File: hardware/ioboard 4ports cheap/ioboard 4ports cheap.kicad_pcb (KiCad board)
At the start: 2 copper layers, 106 x 60 mm, 38 parts, among them J1 Conn_02x06_Odd_Even, J2 Conn_01x03, J3 XLR3, J4 Conn_01x03, J5 XLR3, J6 Conn_01x03, J7 XLR3, J8 Conn_01x03, J9 XLR3, U1 M24C02-WMN, U2 SP3485EN, U3 SP3485EN, U4 SP3485EN, U5 SP3485EN

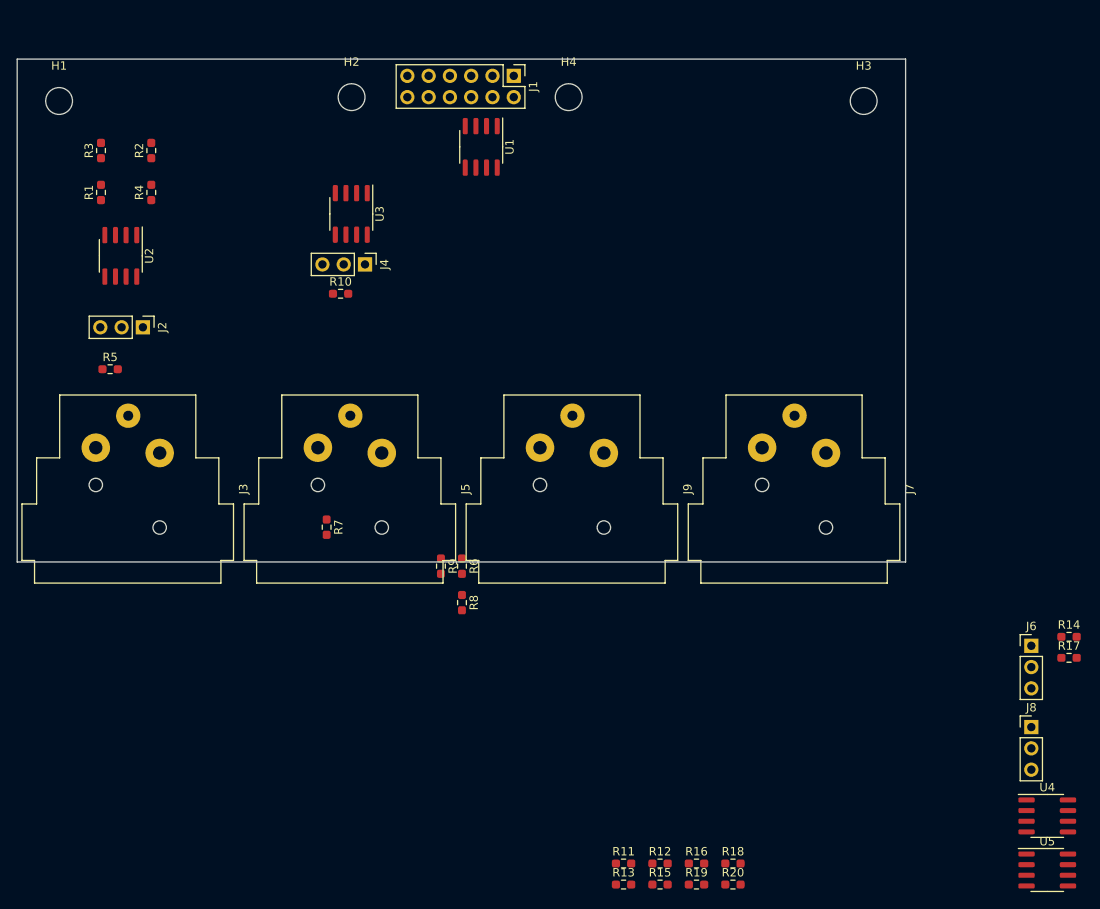
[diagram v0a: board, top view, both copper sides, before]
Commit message: Re-work ioboard 4ports cheap. Should be production-ready
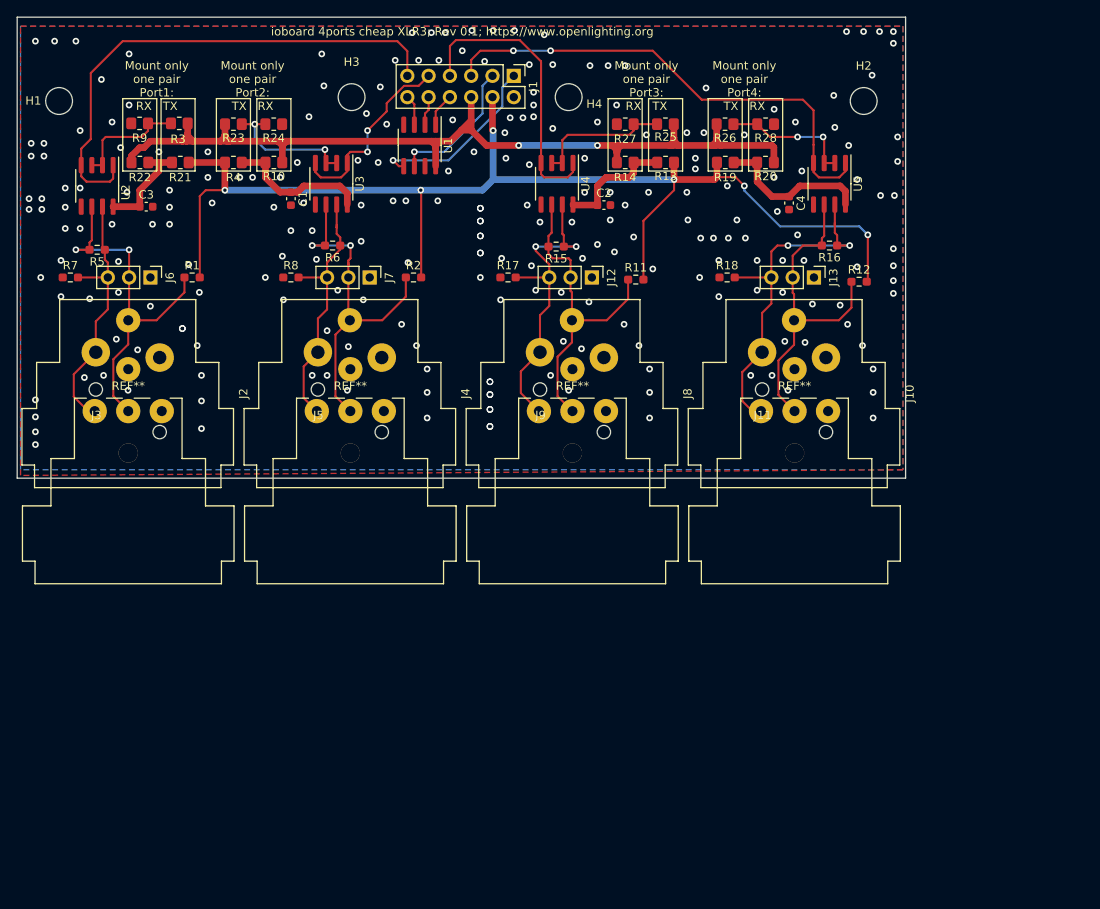
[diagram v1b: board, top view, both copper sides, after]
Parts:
- added C1: 100nF, Capacitor_SMD:C_0603_1608Metric, F.Cu at (57.7, 41.7)
- added C2: 100nF, Capacitor_SMD:C_0603_1608Metric, F.Cu at (95.0, 42.4)
- added C3: 100nF, Capacitor_SMD:C_0603_1608Metric, F.Cu at (40.4, 42.6)
- added C4: 100nF, Capacitor_SMD:C_0603_1608Metric, F.Cu at (117.1, 42.2)
- added J10: XLR3, Connector_Audio:Jack_XLR_Neutrik_NC3FAAH_Horizontal, F.Cu at (121.5, 60.6)
- added J11: XLR3, NC3FD-H:Jack_XLR_Neutrik_NC3FD-H_Horizontal, F.Cu at (117.8, 67.0)
- added J12: Conn_01x03, Connector_PinHeader_2.54mm:PinHeader_1x03_P2.54mm_Vertical, F.Cu at (93.6, 51.1)
- added J13: Conn_01x03, Connector_PinHeader_2.54mm:PinHeader_1x03_P2.54mm_Vertical, F.Cu at (120.1, 51.1)
- added R21: 0R, Resistor_SMD:R_0805_2012Metric_Pad1.20x1.40mm_HandSolder, F.Cu at (44.5, 37.3)
- added R22: 0R-DO_NOT_MOUNT, Resistor_SMD:R_0805_2012Metric_Pad1.20x1.40mm_HandSolder, F.Cu at (39.6, 37.3)
- added R23: 0R, Resistor_SMD:R_0805_2012Metric_Pad1.20x1.40mm_HandSolder, F.Cu at (50.8, 32.8)
- added R24: 0R-DO_NOT_MOUNT, Resistor_SMD:R_0805_2012Metric_Pad1.20x1.40mm_HandSolder, F.Cu at (55.6, 32.8)
- added R25: 0R, Resistor_SMD:R_0805_2012Metric_Pad1.20x1.40mm_HandSolder, F.Cu at (102.3, 32.8)
- added R26: 0R, Resistor_SMD:R_0805_2012Metric_Pad1.20x1.40mm_HandSolder, F.Cu at (109.5, 32.8)
- added R27: 0R-DO_NOT_MOUNT, Resistor_SMD:R_0805_2012Metric_Pad1.20x1.40mm_HandSolder, F.Cu at (97.6, 32.8)
- added R28: 0R-DO_NOT_MOUNT, Resistor_SMD:R_0805_2012Metric_Pad1.20x1.40mm_HandSolder, F.Cu at (114.3, 32.8)
- J2, J4, J8: value Conn_01x03 -> XLR3; footprint Connector_PinHeader_2.54mm:PinHeader_1x03_P2.54mm_Vertical -> Connector_Audio:Jack_XLR_Neutrik_NC3FAAH_Horizontal
- J3, J5, J9: footprint Connector_Audio:Jack_XLR_Neutrik_NC3FAAH_Horizontal -> NC3FD-H:Jack_XLR_Neutrik_NC3FD-H_Horizontal
- J7: value XLR3 -> Conn_01x03; footprint Connector_Audio:Jack_XLR_Neutrik_NC3FAAH_Horizontal -> Connector_PinHeader_2.54mm:PinHeader_1x03_P2.54mm_Vertical
- R1, R11, R18, R8: value 0R -> 680R
- R10, R20: value 120R -> 0R-DO_NOT_MOUNT; footprint Resistor_SMD:R_0603_1608Metric_Pad0.98x0.95mm_HandSolder -> Resistor_SMD:R_0805_2012Metric_Pad1.20x1.40mm_HandSolder
- R12, R17, R2, R7: value 0R-DO_NOT_MOUNT -> 680R
- R13, R14, R3, R9: footprint Resistor_SMD:R_0603_1608Metric_Pad0.98x0.95mm_HandSolder -> Resistor_SMD:R_0805_2012Metric_Pad1.20x1.40mm_HandSolder
- R16, R6: value 0R -> 120R
- R19, R4: value 0R-DO_NOT_MOUNT -> 0R; footprint Resistor_SMD:R_0603_1608Metric_Pad0.98x0.95mm_HandSolder -> Resistor_SMD:R_0805_2012Metric_Pad1.20x1.40mm_HandSolder
- moved J6 113.9 mm to (40.9, 51.1), turned to 270 degrees
- moved U4 95.4 mm to (89.4, 39.9), turned to 270 degrees
- moved R13 86.3 mm to (102.4, 37.3), turned to 180 degrees
- moved R20 86.2 mm to (114.3, 37.3), turned to 180 degrees
- moved R19 86.2 mm to (109.5, 37.3)
- moved U5 85.9 mm to (121.9, 39.9), turned to 270 degrees
- moved R17 80.9 mm to (83.6, 51.1)
- moved R14 77.5 mm to (97.6, 37.3)
- moved R15 77.1 mm to (89.3, 47.4), turned to 180 degrees
- moved R16 75.4 mm to (121.9, 47.2), turned to 180 degrees
- moved R12 73.4 mm to (125.5, 51.6)
- moved R18 69.9 mm to (109.7, 51.1)
- moved R11 69.7 mm to (98.8, 51.3)
- moved J8 67.4 mm to (95.0, 60.6), turned to 270 degrees
- moved R9 63.9 mm to (39.6, 32.7), turned to 0 degrees
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- renumbered H3 to H2, H2 to H3
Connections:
- J2 pad 1: Net-(J2-Pad1) -> GND
- J2 pad 2: GND -> Net-(J2-Pad2)
- J3 pad 2: Net-(J2-Pad3) -> Net-(J2-Pad2)
- J3 pad 3: Net-(J2-Pad1) -> Net-(J2-Pad3)
- J4 pad 1: Net-(J4-Pad1) -> GND
- J4 pad 2: GND -> Net-(J4-Pad2)
- J5 pad 2: Net-(J4-Pad3) -> Net-(J4-Pad2)
- J5 pad 3: Net-(J4-Pad1) -> Net-(J4-Pad3)
- J6 pad 1: Net-(J6-Pad1) -> GND
- J6 pad 2: GND -> Net-(J2-Pad3)
- J6 pad 3: Net-(J6-Pad3) -> Net-(J2-Pad2)
- J7 pad 2: Net-(J6-Pad3) -> Net-(J4-Pad3)
- J7 pad 3: Net-(J6-Pad1) -> Net-(J4-Pad2)
- J8 pad 1: Net-(J8-Pad1) -> GND
- J8 pad 2: GND -> Net-(J12-Pad3)
- J8 pad 3: Net-(J8-Pad3) -> Net-(J12-Pad2)
- J9 pad 2: Net-(J8-Pad3) -> Net-(J12-Pad3)
- J9 pad 3: Net-(J8-Pad1) -> Net-(J12-Pad2)
- R1 pad 1: +5V -> Net-(J2-Pad3)
- R1 pad 2: Net-(R1-Pad2) -> +5V
- R10 pad 1: Net-(J4-Pad3) -> +3V3
- R10 pad 2: Net-(J4-Pad1) -> Net-(C1-Pad1)
- R11 pad 1: Net-(R11-Pad1) -> Net-(J12-Pad2)
- R11 pad 2: +3V3 -> +5V
- R12 pad 1: GND -> Net-(J10-Pad3)
- R12 pad 2: Net-(R11-Pad1) -> +5V
- R13 pad 2: Net-(R13-Pad2) -> Net-(C2-Pad1)
- R14 pad 1: Net-(R13-Pad2) -> +3V3
- R14 pad 2: +3V3 -> Net-(C2-Pad1)
- R15 pad 1: Net-(J6-Pad3) -> Net-(J12-Pad3)
- R15 pad 2: Net-(J6-Pad1) -> Net-(J12-Pad2)
- R16 pad 1: Net-(R16-Pad1) -> Net-(J10-Pad2)
- R16 pad 2: +3V3 -> Net-(J10-Pad3)
- R17 pad 2: Net-(R16-Pad1) -> Net-(J12-Pad3)
- R18 pad 1: +5V -> GND
- R18 pad 2: Net-(R18-Pad2) -> Net-(J10-Pad2)
- R19 pad 1: Net-(R18-Pad2) -> +5V
- R19 pad 2: +3V3 -> Net-(C4-Pad1)
- R2 pad 1: Net-(R1-Pad2) -> Net-(J4-Pad3)
- R2 pad 2: +3V3 -> +5V
- R20 pad 1: Net-(J8-Pad3) -> +3V3
- R20 pad 2: Net-(J8-Pad1) -> Net-(C4-Pad1)
- R4 pad 1: GND -> +5V
- R4 pad 2: Net-(R3-Pad1) -> Net-(C1-Pad1)
- R5 pad 1: Net-(J2-Pad3) -> Net-(J2-Pad2)
- R5 pad 2: Net-(J2-Pad1) -> Net-(J2-Pad3)
- R6 pad 1: Net-(R6-Pad1) -> Net-(J4-Pad2)
- R6 pad 2: +3V3 -> Net-(J4-Pad3)
- R7 pad 2: Net-(R6-Pad1) -> Net-(J2-Pad2)
- R8 pad 1: +5V -> GND
- R8 pad 2: Net-(R8-Pad2) -> Net-(J4-Pad2)
- R9 pad 1: Net-(R8-Pad2) -> GND
- R9 pad 2: +3V3 -> Net-(R3-Pad1)
- U2 pad 6: Net-(J2-Pad1) -> Net-(J2-Pad3)
- U2 pad 7: Net-(J2-Pad3) -> Net-(J2-Pad2)
- U2 pad 8: Net-(R1-Pad2) -> Net-(C3-Pad1)
- U3 pad 2: Net-(R6-Pad1) -> Net-(R23-Pad1)
- U3 pad 3: Net-(R6-Pad1) -> Net-(R23-Pad1)
- U3 pad 6: Net-(J4-Pad1) -> Net-(J4-Pad3)
- U3 pad 7: Net-(J4-Pad3) -> Net-(J4-Pad2)
- U3 pad 8: Net-(R8-Pad2) -> Net-(C1-Pad1)
- U4 pad 1: /GP3 -> /GP2
- U4 pad 2: Net-(R11-Pad1) -> Net-(R25-Pad1)
- U4 pad 3: Net-(R11-Pad1) -> Net-(R25-Pad1)
- U4 pad 4: /GP3 -> /GP2
- U4 pad 6: Net-(J6-Pad1) -> Net-(J12-Pad2)
- U4 pad 7: Net-(J6-Pad3) -> Net-(J12-Pad3)
- U4 pad 8: Net-(R13-Pad2) -> Net-(C2-Pad1)
- U5 pad 1: /GP2 -> /GP3
- U5 pad 2: Net-(R16-Pad1) -> Net-(R26-Pad1)
- U5 pad 3: Net-(R16-Pad1) -> Net-(R26-Pad1)
- U5 pad 4: /GP2 -> /GP3
- U5 pad 6: Net-(J8-Pad1) -> Net-(J10-Pad3)
- U5 pad 7: Net-(J8-Pad3) -> Net-(J10-Pad2)
- U5 pad 8: Net-(R18-Pad2) -> Net-(C4-Pad1)
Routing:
- net +5V: track 0.00 -> 144.1 mm, vias 0 -> 6
- net +3V3: track 0.00 -> 117.7 mm, vias 0 -> 2
- net /GP0: track 0.00 -> 61.4 mm
- net /GP3: track 0.00 -> 58.9 mm, vias 0 -> 2
- net Net-(J2-Pad3): track 0.00 -> 43.9 mm, vias 0 -> 2
- net Net-(J10-Pad2): track 0.00 -> 42.8 mm, vias 0 -> 2
- net Net-(J4-Pad3): track 0.00 -> 42.8 mm, vias 0 -> 2
- net Net-(J10-Pad3): track 0.00 -> 39.7 mm
- net Net-(J12-Pad2): track 0.00 -> 38.6 mm
- net Net-(J12-Pad3): track 0.00 -> 38.0 mm, vias 0 -> 2
- net /GP2: track 0.00 -> 33.6 mm
- net Net-(J2-Pad2): track 0.00 -> 31.4 mm
- net Net-(J4-Pad2): track 0.00 -> 31.0 mm
- net /GP1: track 0.00 -> 23.1 mm, vias 0 -> 2
- net /SDA: track 0.00 -> 21.5 mm, vias 0 -> 1
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- added copper zone on B.Cu, net GND
- added copper zone on F.Cu, net GND
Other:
- board size 106 x 60 mm -> 106 x 55 mm
- board text added: "Mount only one pair Port1: RX TX"
- board text added: "Mount only one pair Port2: TX RX"
- board text added: "Mount only one pair Port3: RX TX"
- board text added: "Mount only one pair Port4: TX RX"
- board text added: "ioboard 4ports cheap XLR3; Rev 0.1; https://www.openlighting.org"
